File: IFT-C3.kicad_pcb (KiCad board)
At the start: 2 copper layers, 85.6 x 54 mm, 54 parts, among them IC1 DIO5508XS8, J2 Conn_01x10_Pin, J3 USB4085-GF-A_REVB, J4 Conn_01x10_Pin, J5 SJ-3523-SMT-TR, J7 Conn_01x02, Q1 Q_Photo_NPN, U1 AZ1117-3.3, U2 ESP32-C3-WROOM-02

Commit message: WIP v2024
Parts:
- removed REF**: KiCad-Logo2_12mm_SilkScreen, Symbol:KiCad-Logo2_12mm_SilkScreen
- removed S1, S2: PTS526_SMG15J_SMTR2_LFS, Local footprints:PTS526SMG15JSMTR2LFS
- added D10: 1N4148WS, Diode_SMD:D_SOD-323_HandSoldering, F.Cu at (122.4, -5.78)
- added D11: 1N4148WS, Diode_SMD:D_SOD-323_HandSoldering, F.Cu at (122.4, -2.83)
- added D12: 1N4148WS, Diode_SMD:D_SOD-323_HandSoldering, F.Cu at (122.4, 0.12)
- added D13: 1N4148WS, Diode_SMD:D_SOD-323_HandSoldering, F.Cu at (122.4, 3.07)
- added D6: 1N4148WS, Diode_SMD:D_SOD-323_HandSoldering, F.Cu at (122.4, -17.6)
- added D7: 1N4148WS, Diode_SMD:D_SOD-323_HandSoldering, F.Cu at (122.4, -14.6)
- added D8: 1N4148WS, Diode_SMD:D_SOD-323_HandSoldering, F.Cu at (122.4, -11.7)
- added D9: 1N4148WS, Diode_SMD:D_SOD-323_HandSoldering, F.Cu at (122.4, -8.73)
- added J1: Conn_01x04_Socket, footprints:SSD1306_module, F.Cu at (52.7, 43.0)
- added SW1: SW_Push_Dual, footprints:PTS526SM15SMTR2LFS, F.Cu at (77.1, 30.7)
- added SW10: SW_Push_Dual, footprints:PTS526SM15SMTR2LFS, F.Cu at (64.5, 110.0)
- added SW3: SW_Push_Dual, footprints:PTS526SM15SMTR2LFS, F.Cu at (39.1, 77.8)
- added SW4: SW_Push_Dual, footprints:PTS526SM15SMTR2LFS, F.Cu at (47.1, 85.8)
- added SW5: SW_Push_Dual, footprints:PTS526SM15SMTR2LFS, F.Cu at (74.9, 81.5)
- added SW6: SW_Push_Dual, footprints:PTS526SM15SMTR2LFS, F.Cu at (31.1, 85.8)
- added SW7: SW_Push_Dual, footprints:PTS526SM15SMTR2LFS, F.Cu at (42.0, 110.0)
- added SW8: SW_Push_Dual, footprints:PTS526SM15SMTR2LFS, F.Cu at (65.1, 85.8)
- added SW9: SW_Push_Dual, footprints:PTS526SM15SMTR2LFS, F.Cu at (39.1, 93.8)
- added U3: MAX98357A, Package_DFN_QFN:TQFN-16-1EP_3x3mm_P0.5mm_EP1.23x1.23mm, B.Cu at (71.2, 86.6)
- C10, C11, C3, C4, C5, C8, C9, D2, D3, FB1, IC1, J2, J3, J4, J5, J7, JP1, JP2, JP6, R1, R10, R2, R3, R6, R7, R8, R9, S3, U2: moved to B.Cu
- moved G*** 164.3 mm to (-39.5, 66.7), turned to -90 degrees
- moved Q1 137.6 mm to (16.4, 17.8), turned to 180 degrees
- moved R11 134.0 mm to (15.4, 21.3), turned to -90 degrees
- moved JP3 132.6 mm to (17.4, 21.3), turned to 90 degrees
- moved C5 115.2 mm to (28.7, 30.1), turned to 90 degrees
- moved C4 111.3 mm to (30.8, 31.2), turned to 90 degrees
- moved C3 102.7 mm to (35.7, 33.8), turned to 180 degrees
- moved R3 100.2 mm to (35.7, 36.1), turned to 180 degrees
- moved U2 99.8 mm to (39.7, 49.0)
- moved J4 87.9 mm to (21.0, 50.5), turned to 180 degrees
- moved R7 80.3 mm to (28.7, 79.9), turned to -90 degrees
- moved D3 78.4 mm to (28.7, 83.7), turned to 90 degrees
- moved R6 77.8 mm to (32.7, 81.2), turned to -90 degrees
- moved S3 77.2 mm to (29.1, 94.2), turned to 90 degrees
- moved D2 76.4 mm to (32.7, 85.0), turned to 90 degrees
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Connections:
- net /Button/NO renamed Net-(U2-EN/CHIP_PU)
- C1 pad 1: +BATT -> +BATT_after_switch
- J7 pad 1: Net-(J7-Pin_1) -> +BATT
- S3 pad C1: Net-(J7-Pin_1) -> +BATT_after_switch
- U1 pad 3: +BATT -> +BATT_after_switch
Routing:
- net +3.3V: track 119.1 -> 0.00 mm, vias 5 -> 0
- net /D+: track 73.5 -> 0.00 mm
- net /D-: track 72.0 -> 0.00 mm
- net VBUS: track 71.9 -> 0.00 mm
- net +BATT: track 69.5 -> 0.00 mm, vias 3 -> 0
- net /GPIO9: track 60.4 -> 0.00 mm, vias 2 -> 0
- net /GPIO2: track 58.4 -> 0.00 mm
- net /GPIO3: track 57.6 -> 0.00 mm
- net /GPIO1: track 56.8 -> 0.00 mm, vias 2 -> 0
- net GND: track 43.6 -> 0.00 mm, vias 28 -> 0
- net Net-(U2-EN/CHIP_PU): track 28.1 -> 0.00 mm
- net Net-(D4-DIN): track 24.4 -> 0.00 mm
- net /GPIO4: track 21.1 -> 0.00 mm, vias 2 -> 0
- net Net-(FB1-Pad1): track 20.5 -> 0.00 mm
- net /Rx: track 20.2 -> 0.00 mm
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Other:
- board size 85.6 x 54 mm -> 54 x 88.7 mm

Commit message: WIP, routed
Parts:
- removed D3: LED, Diode_SMD:D_0805_2012Metric_Pad1.15x1.40mm_HandSolder
- removed the G001 at (133.8, 95.0)
- removed G002, G003: LOGO, Local footprints:segments
- removed R7: 10K, Resistor_SMD:R_0805_2012Metric_Pad1.20x1.40mm_HandSolder
- removed U3: MAX98357A, Package_DFN_QFN:TQFN-16-1EP_3x3mm_P0.5mm_EP1.23x1.23mm
- added G001: LOGO, Segments:segments, B.Cu at (70.4, 76.7)
- added G001: LOGO, Segments:segments, B.Cu at (70.4, 83.8)
- added G001: LOGO, Segments:segments, B.Cu at (70.3, 91.0)
- added JP7: SolderJumper_2_Open, Jumper:SolderJumper-2_P1.3mm_Open_TrianglePad1.0x1.5mm, B.Cu at (57.8, 70.6)
- added Q2: Q_NMOS_GSD, Package_TO_SOT_SMD:SOT-23-3, B.Cu at (53.2, 72.2)
- added R14: 10k, Resistor_SMD:R_0805_2012Metric_Pad1.20x1.40mm_HandSolder, B.Cu at (46.6, 71.4)
- added REF**: Fiducial_0.5mm_Mask1.5mm, Fiducial:Fiducial_0.5mm_Mask1.5mm, F.Cu at (28.1, 114.7)
- added REF**: Fiducial_0.5mm_Mask1.5mm, Fiducial:Fiducial_0.5mm_Mask1.5mm, B.Cu at (28.1, 114.7)
- C1: value 10u -> 22u; moved to B.Cu
- C2, C6, C7, JP3, JP4, JP5, R12, R13, R4, R5, SW1: moved to B.Cu
- D2: moved to F.Cu
- R11: footprint Resistor_SMD:R_0603_1608Metric -> Resistor_SMD:R_0805_2012Metric_Pad1.20x1.40mm_HandSolder; moved to B.Cu
- U1: value AZ1117-3.3 -> AZ1117CR-3.3TRG1; moved to B.Cu
- moved D10 137.2 mm to (42.0, 105.4)
- moved D9 127.7 mm to (31.0, 80.5), turned to 180 degrees
- moved D6 122.1 mm to (44.5, 76.5), turned to 90 degrees
- moved D12 121.5 mm to (44.8, 93.7), turned to 90 degrees
- moved D7 120.6 mm to (48.1, 80.4), turned to 180 degrees
- moved D13 117.4 mm to (64.5, 105.2)
- moved D11 104.5 mm to (60.7, 81.6), turned to 25 degrees
- moved D8 101.8 mm to (72.8, 77.2), turned to 25 degrees
- moved G*** 93.0 mm to (52.3, 81.2), turned to 180 degrees
- moved C6 87.2 mm to (39.1, 85.8), turned to 180 degrees
- moved D5 70.6 mm to (39.1, 85.8)
- moved R5 67.2 mm to (40.4, 34.5)
- moved D1 66.4 mm to (42.7, 35.1), turned to 180 degrees
- moved S3 64.7 mm to (53.0, 34.0), turned to 0 degrees
- moved J7 64.6 mm to (31.3, 40.7), turned to -90 degrees
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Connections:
- net /GPIO2 renamed Audio_L
- net /GPIO3 renamed Audio_R
- D10 pad 1: /Keyboard Matrix/I_2 -> I_2
- D11 pad 1: /Keyboard Matrix/I_2 -> I_2
- D12 pad 1: /Keyboard Matrix/I_3 -> Batt_mon
- D13 pad 1: /Keyboard Matrix/I_3 -> Batt_mon
- D6 pad 1: /Keyboard Matrix/I_1 -> I_1
- D7 pad 1: /Keyboard Matrix/I_1 -> I_1
- D8 pad 1: /Keyboard Matrix/I_1 -> I_1
- D9 pad 1: /Keyboard Matrix/I_2 -> I_2
- J1 pad 3: /SCL -> SCL
- J1 pad 4: /SDA -> SDA
- J2 pad 1: /GPIO0 -> O_3
- J2 pad 2: /GPIO1 -> Batt_mon
- J2 pad 5: /GPIO10 -> Photo_Tr
- J2 pad 7: /Rx -> O_1
- J4 pad 3: GND -> Tr_DRAIN
- J4 pad 4: /GPIO9 -> O_2
- J4 pad 5: /GPIO8 -> RGB_LEDs
- J4 pad 6: /GPIO7 -> I_2
- J4 pad 7: /GPIO6 -> I_1
- J4 pad 8: /GPIO5 -> SCL
- J4 pad 9: /GPIO4 -> SDA
- JP3 pad 1: /GPIO4 -> Photo_Tr
- JP4 pad 1: /GPIO1 -> Batt_mon
- JP5 pad 1: /GPIO10 -> RGB_LEDs
- S3 pad MP1: unconnected-(S3-PadMP1) -> GND
- S3 pad MP2: unconnected-(S3-PadMP2) -> GND
- S3 pad MP3: unconnected-(S3-PadMP3) -> GND
- S3 pad MP4: unconnected-(S3-PadMP4) -> GND
- SW10 pad 1: /Keyboard Matrix/O_2 -> O_2
- SW10 pad 3: /GPIO9 -> RGB_LEDs
- SW3 pad 1: /Keyboard Matrix/O_1 -> O_1
- SW3 pad 3: /Keyboard Matrix/O_1 -> O_1
- SW4 pad 1: /Keyboard Matrix/O_2 -> O_2
- SW4 pad 3: /Keyboard Matrix/O_2 -> O_2
- SW5 pad 1: /Keyboard Matrix/O_3 -> O_3
- SW5 pad 3: /Keyboard Matrix/O_3 -> O_3
- SW6 pad 1: /Keyboard Matrix/O_1 -> O_1
- SW6 pad 3: /Keyboard Matrix/O_1 -> O_1
- SW7 pad 1: /Keyboard Matrix/O_2 -> O_2
- SW7 pad 3: /Keyboard Matrix/O_2 -> O_2
- SW8 pad 1: /Keyboard Matrix/O_3 -> O_3
- SW8 pad 3: /Keyboard Matrix/O_3 -> O_3
- SW9 pad 1: /Keyboard Matrix/O_1 -> O_1
- SW9 pad 3: /Keyboard Matrix/O_1 -> O_1
- U2 pad 10: /GPIO10 -> O_2
- U2 pad 11: /Rx -> O_1
- U2 pad 17: /GPIO1 -> Batt_mon
- U2 pad 18: /GPIO0 -> O_3
- U2 pad 3: /GPIO4 -> Photo_Tr
- U2 pad 4: /GPIO5 -> SDA
- U2 pad 5: /GPIO6 -> SCL
- U2 pad 6: /GPIO7 -> I_1
- U2 pad 7: /GPIO8 -> I_2
- U2 pad 8: /GPIO9 -> RGB_LEDs
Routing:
- net +3.3V: track 0.00 -> 178.6 mm, vias 0 -> 9
- net GND: track 0.00 -> 134.6 mm, vias 0 -> 31
- net Batt_mon: track 0.00 -> 131.3 mm, vias 0 -> 3
- net VBUS: track 0.00 -> 113.6 mm, vias 0 -> 4
- net O_2: track 0.00 -> 112.1 mm, vias 0 -> 3
- net Net-(U2-EN/CHIP_PU): track 0.00 -> 111.7 mm, vias 0 -> 2
- net O_1: track 0.00 -> 106.1 mm, vias 0 -> 2
- net RGB_LEDs: track 0.00 -> 104.8 mm, vias 0 -> 3
- net Photo_Tr: track 0.00 -> 98.9 mm, vias 0 -> 3
- net SDA: track 0.00 -> 89.0 mm, vias 0 -> 2
- net Audio_R: track 0.00 -> 84.8 mm
- net SCL: track 0.00 -> 83.6 mm, vias 0 -> 2
- net I_2: track 0.00 -> 82.2 mm, vias 0 -> 5
- net I_1: track 0.00 -> 77.0 mm, vias 0 -> 4
- net Net-(D4-DO): track 0.00 -> 76.2 mm, vias 0 -> 2
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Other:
- board size 54 x 88.7 mm -> 54 x 85.6 mm
- board text added: "+"
- board text added: "-"
- board text added: "0/O_3"
- board text added: "1/Batt_mon"
- board text added: "10/O_2"
- board text added: "2/Audio_L"
- board text added: "20/Rx/O_1"
- board text added: "2024"
- board text added: "21/Tx"
- board text added: "3/Audio_R"
- board text added: "4/Photo_Tr"
- board text added: "5/SDA"
- board text added: "6/SCL"
- board text added: "7/I_1"
- board text added: "8/I_2"
- board text added: "9/RGB"
- board text added: "Ambiant Light Sensor"
- board text added: "MOSFET Output"
- board text added: "RGB LEDs"
- board text added: "RGB_Out"
- board text added: "Tr_Drain"
- board text removed: "0"
- board text removed: "1"
- board text removed: "10"
- board text removed: "2"
- board text removed: "20/Tx"
- board text removed: "21/Rx"
- board text removed: "3"
- board text removed: "4"
- board text removed: "5"
- board text removed: "6"
- board text removed: "7"
- board text removed: "8"
- board text removed: "9"
- board text removed: "Ambiant Light"
- board text removed: "Done"
- board text removed: "RGB LED"
- board text removed: "RGB_O"
- board text removed: "September 2023"

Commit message: holes cleared
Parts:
- removed the G001 at (70.4, 76.7)
- removed the G001 at (70.4, 83.8)
- removed the G001 at (70.3, 91.0)
- added G001: LOGO, footprints:segments, B.Cu at (68.7, 90.3)
- added G001: LOGO, footprints:segments, B.Cu at (68.9, 76.0)
- added G001: LOGO, footprints:segments, B.Cu at (68.8, 83.1)
- moved C8 14.3 mm to (75.6, 105.5)
- moved C9 14.2 mm to (75.6, 101.0)
- moved R9 14.1 mm to (75.6, 96.6)
- moved JP1 13.8 mm to (75.3, 92.8)
- moved G*** 5.45 mm to (69.8, 96.8)
- moved C10 3.28 mm to (77.8, 105.5)
- moved C11 2.94 mm to (77.9, 101.0)
- moved R10 2.32 mm to (77.9, 96.6)
- moved J5 2.00 mm to (68.3, 113.5)
- moved FB1 1.80 mm to (59.5, 109.7)
- moved JP2 1.73 mm to (77.9, 92.8)
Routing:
- net Net-(FB1-Pad1): track 0.00 -> 30.4 mm
- net Audio_L: track 72.1 -> 86.6 mm, vias 1 -> 3
- net GND: track 134.6 -> 126.1 mm
- net /PWM_filter/Out: track 6.17 -> 11.1 mm
- net Audio_R: track 84.8 -> 88.8 mm, vias 0 -> 3
- net /PWM_filter1/Out: track 8.94 -> 12.8 mm
- net Photo_Tr: track 98.9 -> 96.7 mm
- net Net-(C8-Pad1): track 10.6 -> 8.54 mm
- net /PWM_filter1/In: track 2.59 -> 1.88 mm
- net I_1: track 77.0 -> 77.6 mm
- net RGB_LEDs: track 104.8 -> 105.4 mm
- net Net-(C10-Pad1): track 8.88 -> 8.58 mm, vias 0 -> 2
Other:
- outline, holes or cut-outs redrawn
- board text added: "A"
- board text added: "B"
- board text added: "Boot/Start"
- board text added: "Select"
- board text removed: "Boot"

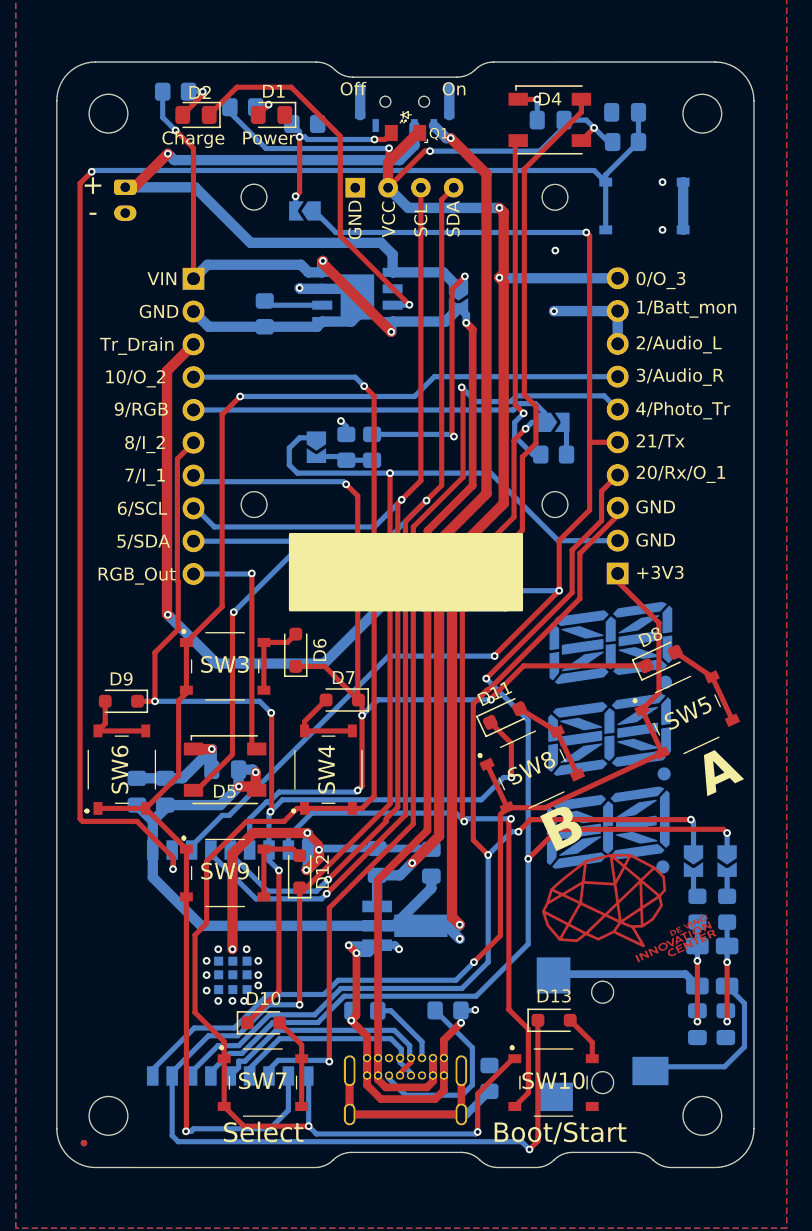
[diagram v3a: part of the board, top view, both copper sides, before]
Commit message: RGB LEDs moved, almost ready for prob
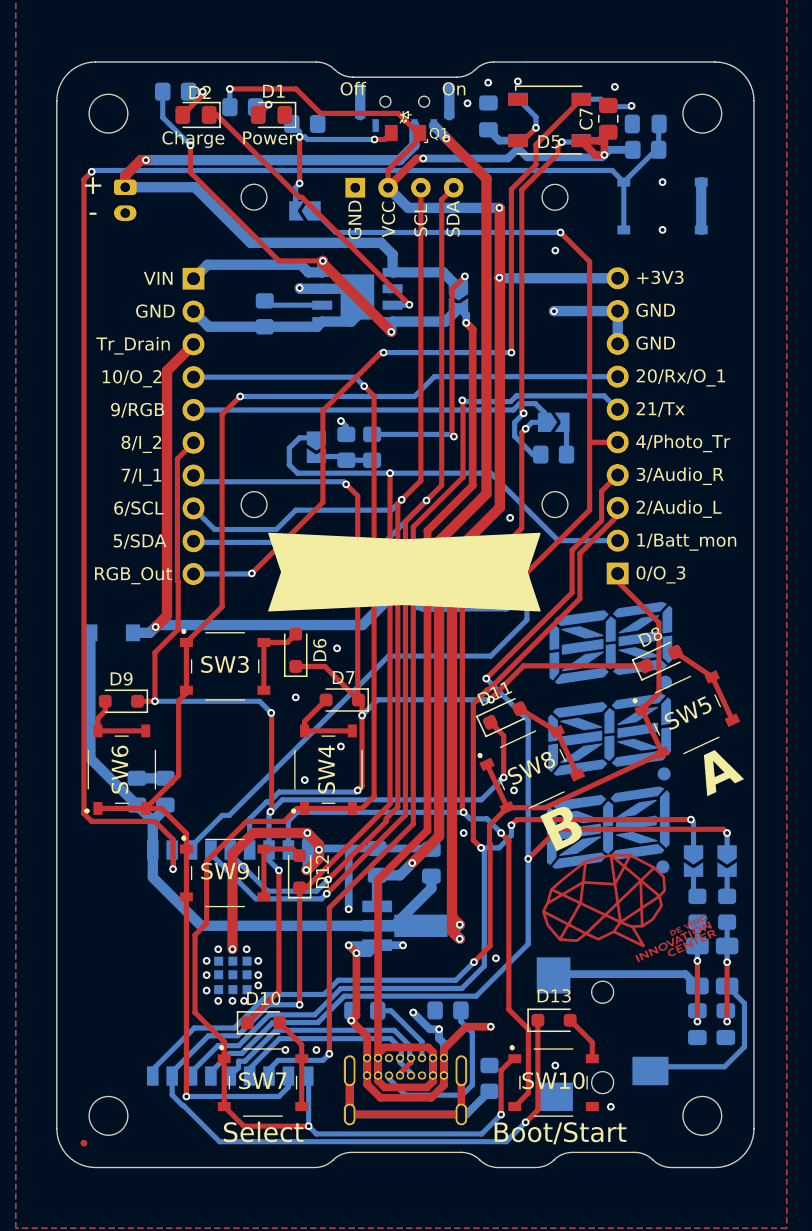
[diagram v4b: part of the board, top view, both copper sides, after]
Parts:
- added J6: Conn_01x02_Pin, Motors:Vybronics_VZ30C1T8219732L, B.Cu at (30.3, 79.5)
- C7: moved to F.Cu
- D4: moved to B.Cu
- moved D5 56.2 mm to (64.2, 35.5)
- moved C6 54.5 mm to (59.5, 35.2), turned to 90 degrees
- moved C7 4.46 mm to (68.7, 35.4), turned to 90 degrees
- moved C3 1.84 mm to (71.6, 35.8)
- moved R3 1.67 mm to (71.6, 37.8)
- moved SW1 1.40 mm to (72.9, 42.1)
- turned D4 to 180 degrees
- turned R2 to 180 degrees
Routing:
- net Net-(D4-DO): track 76.2 -> 4.60 mm, vias 2 -> 1
- net /RGB_OUT: track 18.3 -> 57.7 mm, vias 1 -> 3
- net +3.3V: track 178.6 -> 191.9 mm, vias 9 -> 7
- net VBUS: track 113.6 -> 123.8 mm
- net /Charge: track 29.2 -> 22.9 mm
- net O_1: track 106.1 -> 101.9 mm
- net Photo_Tr: track 96.7 -> 92.8 mm, vias 3 -> 2
- net Batt_mon: track 131.3 -> 127.5 mm
- net GND: track 126.1 -> 128.8 mm, vias 31 -> 49
- net Net-(D4-DIN): track 26.2 -> 28.6 mm, vias 1 -> 2
- net /Tx: track 75.2 -> 73.3 mm
- net Tr_DRAIN: track 43.1 -> 44.5 mm
- net RGB_LEDs: track 105.4 -> 104.0 mm
- net Net-(U2-EN/CHIP_PU): track 111.7 -> 112.6 mm
- net I_2: track 82.2 -> 81.3 mm
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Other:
- board text added: "v2024"
- board text removed: "2024"

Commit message: Version sent to Aisler
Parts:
- moved J6 3.25 mm to (33.2, 81.0)
- moved C5 2.15 mm to (30.3, 88.4), turned to 180 degrees
- moved G*** 1.66 mm to (50.7, 81.2)
- moved C4 1.66 mm to (35.8, 88.4), turned to 0 degrees
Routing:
- net GND: track 128.8 -> 126.6 mm, vias 49 -> 53
- net +3.3V: track 191.9 -> 190.1 mm
- net Tr_DRAIN: track 44.5 -> 45.1 mm
- net Net-(U2-EN/CHIP_PU): track 112.6 -> 112.8 mm, vias 2 -> 4
